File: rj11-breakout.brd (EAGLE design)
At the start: 100 x 80 mm, 2 parts, among them J1 22-27-2061-06, X1 XRJK-S-01-6-6-0-2G2-NO

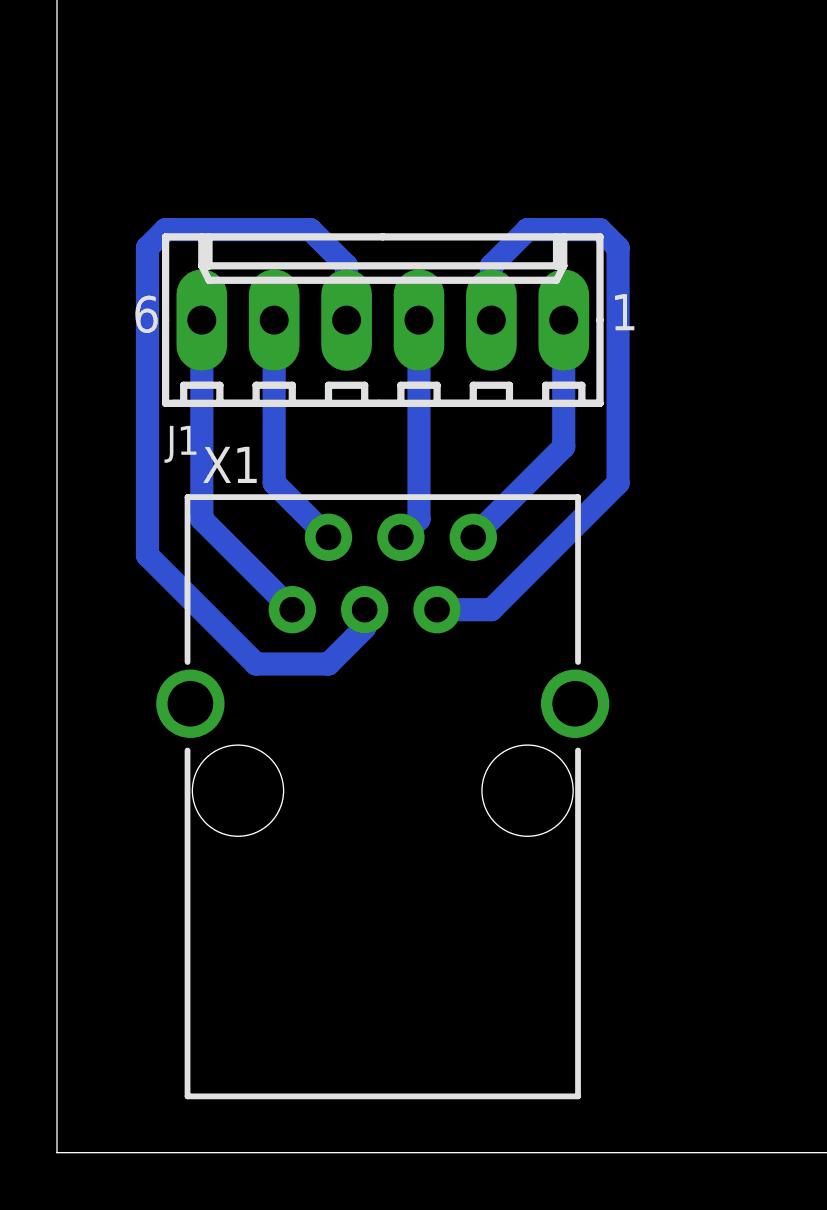
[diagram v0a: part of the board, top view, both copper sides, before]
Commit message: New RJ11 breakout
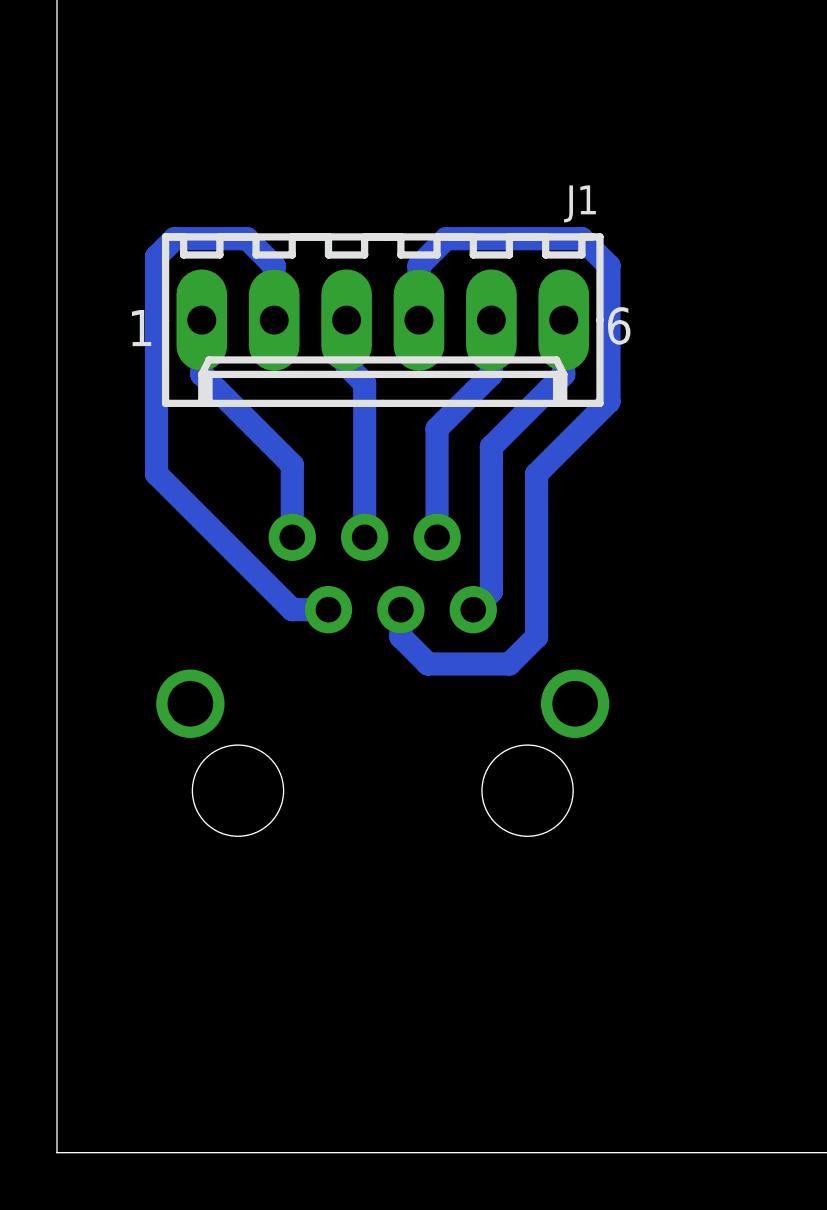
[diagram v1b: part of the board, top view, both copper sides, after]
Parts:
- turned J1 to 180 degrees
- flipped X1 to the bottom
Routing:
- net N$5: track 23.6 -> 22.3 mm
- net N$3: track 30.8 -> 29.9 mm
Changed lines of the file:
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@@
 <setting verticaltext="up"/>
 </settings>
-<grid distance="0.025" unitdist="inch" unit="inch" style="lines" multiple="1" display="no" altdistance="0.025" altunitdist="inch" altunit="inch"/>
+<grid distance="0.0125" unitdist="inch" unit="inch" style="lines" multiple="1" display="no" altdistance="0.025" altunitdist="inch" altunit="inch"/>
 <layers>
 <layer number="1" name="Top" color="4" fill="1" visible="yes" active="yes"/>
@@
 </autorouter>
 <elements>
-<element name="X1" library="con-xmultiple" package="XRJK-S-01-6-6-0-2G2-NO" value="XRJK-S-01-6-6-0-2G2-NO" x="11.43" y="12.7"/>
-<element name="J1" library="con-molex" package="6410-06" value="22-27-2061-06" x="11.43" y="29.21">
-<attribute name="OC_NEWARK" value="unknown" x="34.29" y="0" size="1.778" layer="27" display="off"/>
-<attribute name="MPN" value="" x="34.29" y="0" size="1.778" layer="27" display="off"/>
-<attribute name="MF" value="" x="34.29" y="0" size="1.778" layer="27" display="off"/>
-<attribute name="OC_FARNELL" value="unknown" x="34.29" y="0" size="1.778" layer="27" display="off"/>
+<element name="X1" library="con-xmultiple" package="XRJK-S-01-6-6-0-2G2-NO" value="XRJK-S-01-6-6-0-2G2-NO" x="11.43" y="12.7" rot="MR0"/>
+<element name="J1" library="con-molex" package="6410-06" value="22-27-2061-06" x="11.43" y="29.21" rot="R180">
+<attribute name="OC_NEWARK" value="unknown" x="-11.43" y="58.42" size="1.778" layer="27" rot="R180" display="off"/>
+<attribute name="MPN" value="" x="-11.43" y="58.42" size="1.778" layer="27" rot="R180" display="off"/>
+<attribute name="MF" value="" x="-11.43" y="58.42" size="1.778" layer="27" rot="R180" display="off"/>
+<attribute name="OC_FARNELL" value="unknown" x="-11.43" y="58.42" size="1.778" layer="27" rot="R180" display="off"/>
 </element>
 </elements>
@@
 <contactref element="X1" pad="1"/>
 <contactref element="J1" pad="6"/>
-<wire x1="5.08" y1="29.21" x2="5.08" y2="22.225" width="0.8128" layer="16"/>
-<wire x1="5.08" y1="22.225" x2="8.255" y2="19.05" width="0.8128" layer="16"/>
+<wire x1="14.605" y1="19.05" x2="15.24" y2="19.685" width="0.8128" layer="16"/>
+<wire x1="15.24" y1="19.685" x2="15.24" y2="24.765" width="0.8128" layer="16"/>
+<wire x1="15.24" y1="24.765" x2="17.78" y2="27.305" width="0.8128" layer="16"/>
+<wire x1="17.78" y1="27.305" x2="17.78" y2="29.21" width="0.8128" layer="16"/>
 </signal>
 <signal name="N$2">
 <contactref element="X1" pad="2"/>
 <contactref element="J1" pad="5"/>
-<wire x1="7.62" y1="29.21" x2="7.62" y2="23.495" width="0.8128" layer="16"/>
-<wire x1="7.62" y1="23.495" x2="9.525" y2="21.59" width="0.8128" layer="16"/>
+<wire x1="13.335" y1="21.59" x2="13.335" y2="25.4" width="0.8128" layer="16"/>
+<wire x1="13.335" y1="25.4" x2="15.24" y2="27.305" width="0.8128" layer="16"/>
+<wire x1="15.24" y1="27.305" x2="15.24" y2="29.21" width="0.8128" layer="16"/>
 </signal>
 <signal name="N$3">
 <contactref element="X1" pad="3"/>
 <contactref element="J1" pad="4"/>
-<wire x1="10.795" y1="19.05" x2="10.795" y2="18.415" width="0.8128" layer="16"/>
-<wire x1="10.795" y1="18.415" x2="9.525" y2="17.145" width="0.8128" layer="16"/>
-<wire x1="9.525" y1="17.145" x2="6.985" y2="17.145" width="0.8128" layer="16"/>
-<wire x1="6.985" y1="17.145" x2="3.175" y2="20.955" width="0.8128" layer="16"/>
-<wire x1="3.175" y1="20.955" x2="3.175" y2="31.75" width="0.8128" layer="16"/>
-<wire x1="3.175" y1="31.75" x2="3.81" y2="32.385" width="0.8128" layer="16"/>
-<wire x1="3.81" y1="32.385" x2="8.89" y2="32.385" width="0.8128" layer="16"/>
-<wire x1="8.89" y1="32.385" x2="10.16" y2="31.115" width="0.8128" layer="16"/>
-<wire x1="10.16" y1="31.115" x2="10.16" y2="29.21" width="0.8128" layer="16"/>
+<wire x1="12.065" y1="19.05" x2="12.065" y2="18.0975" width="0.8128" layer="16"/>
+<wire x1="12.065" y1="18.0975" x2="13.0175" y2="17.145" width="0.8128" layer="16"/>
+<wire x1="13.0175" y1="17.145" x2="15.875" y2="17.145" width="0.8128" layer="16"/>
+<wire x1="15.875" y1="17.145" x2="16.8275" y2="18.0975" width="0.8128" layer="16"/>
+<wire x1="16.8275" y1="18.0975" x2="16.8275" y2="23.8125" width="0.8128" layer="16"/>
+<wire x1="16.8275" y1="23.8125" x2="19.3675" y2="26.3525" width="0.8128" layer="16"/>
+<wire x1="19.3675" y1="26.3525" x2="19.3675" y2="31.115" width="0.8128" layer="16"/>
+<wire x1="19.3675" y1="31.115" x2="18.415" y2="32.0675" width="0.8128" layer="16"/>
+<wire x1="18.415" y1="32.0675" x2="13.6525" y2="32.0675" width="0.8128" layer="16"/>
+<wire x1="13.6525" y1="32.0675" x2="12.7" y2="31.115" width="0.8128" layer="16"/>
+<wire x1="12.7" y1="31.115" x2="12.7" y2="29.21" width="0.8128" layer="16"/>
 </signal>
 <signal name="N$4">
 <contactref element="X1" pad="4"/>
 <contactref element="J1" pad="3"/>
-<wire x1="12.7" y1="29.21" x2="12.7" y2="22.225" width="0.8128" layer="16"/>
-<wire x1="12.7" y1="22.225" x2="12.065" y2="21.59" width="0.8128" layer="16"/>
+<wire x1="10.16" y1="29.21" x2="10.16" y2="27.6225" width="0.8128" layer="16"/>
+<wire x1="10.16" y1="27.6225" x2="10.795" y2="26.9875" width="0.8128" layer="16"/>
+<wire x1="10.795" y1="26.9875" x2="10.795" y2="21.59" width="0.8128" layer="16"/>
 </signal>
 <signal name="N$5">
 <contactref element="X1" pad="5"/>
 <contactref element="J1" pad="2"/>
-<wire x1="13.335" y1="19.05" x2="15.24" y2="19.05" width="0.8128" layer="16"/>
-<wire x1="15.24" y1="19.05" x2="19.685" y2="23.495" width="0.8128" layer="16"/>
-<wire x1="19.685" y1="23.495" x2="19.685" y2="31.75" width="0.8128" layer="16"/>
-<wire x1="19.685" y1="31.75" x2="19.05" y2="32.385" width="0.8128" layer="16"/>
-<wire x1="19.05" y1="32.385" x2="16.51" y2="32.385" width="0.8128" layer="16"/>
-<wire x1="16.51" y1="32.385" x2="15.24" y2="31.115" width="0.8128" layer="16"/>
-<wire x1="15.24" y1="31.115" x2="15.24" y2="29.21" width="0.8128" layer="16"/>
+<wire x1="9.525" y1="19.05" x2="8.255" y2="19.05" width="0.8128" layer="16"/>
+<wire x1="8.255" y1="19.05" x2="3.4925" y2="23.8125" width="0.8128" layer="16"/>
+<wire x1="3.4925" y1="23.8125" x2="3.4925" y2="31.4325" width="0.8128" layer="16"/>
+<wire x1="3.4925" y1="31.4325" x2="4.1275" y2="32.0675" width="0.8128" layer="16"/>
+<wire x1="4.1275" y1="32.0675" x2="6.6675" y2="32.0675" width="0.8128" layer="16"/>
+<wire x1="6.6675" y1="32.0675" x2="7.62" y2="31.115" width="0.8128" layer="16"/>
+<wire x1="7.62" y1="31.115" x2="7.62" y2="29.21" width="0.8128" layer="16"/>
 </signal>
 <signal name="N$6">
 <contactref element="X1" pad="6"/>
 <contactref element="J1" pad="1"/>
-<wire x1="17.78" y1="29.21" x2="17.78" y2="24.765" width="0.8128" layer="16"/>
-<wire x1="17.78" y1="24.765" x2="14.605" y2="21.59" width="0.8128" layer="16"/>
+<wire x1="8.255" y1="21.59" x2="8.255" y2="24.13" width="0.8128" layer="16"/>
+<wire x1="8.255" y1="24.13" x2="5.08" y2="27.305" width="0.8128" layer="16"/>
+<wire x1="5.08" y1="27.305" x2="5.08" y2="29.21" width="0.8128" layer="16"/>
 </signal>
 </signals>
+<errors>
+</errors>
 </board>
 </drawing>
